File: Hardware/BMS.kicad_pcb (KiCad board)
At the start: 4 copper layers, 109 x 148 mm, 368 parts, among them IC1 STM32H742VIT6, IC2 TPS563200DDCR, J1 Conn_01x28, J10 Conn_01x10, J11 USB4235-03-C_REVA, J13 USB_A, J16 Conn_01x10, J19 Conn_02x13_Counter_Clockwise, J7 FTSH-107-01-L-D-K, Q2 100V/2W, Q5 DMT6018LDR-7, Q7 DMT6018LDR-7, Q8 100V/2W, SW1 SW_Push, U1 BQ79614PAPRQ1, U2 BQ79614PAPRQ1, U3 PBQ79600PWQ1, U4 MCP2542FD-E/MF, U5 PTPSM863253RDXR

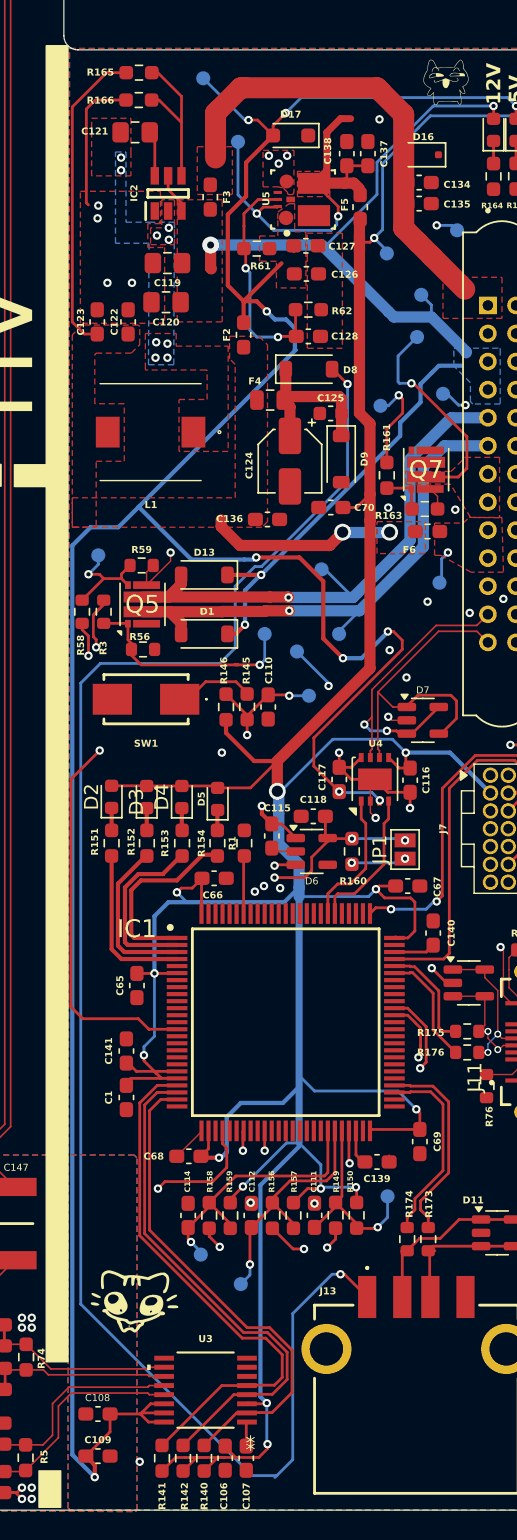
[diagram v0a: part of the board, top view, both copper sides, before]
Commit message: Dodano logikę ładowania bateri, zabezpieczenia OV UV na przekaźniku działają poprawnie, przekaźnik ma swój test polegający na styku pomocniczym
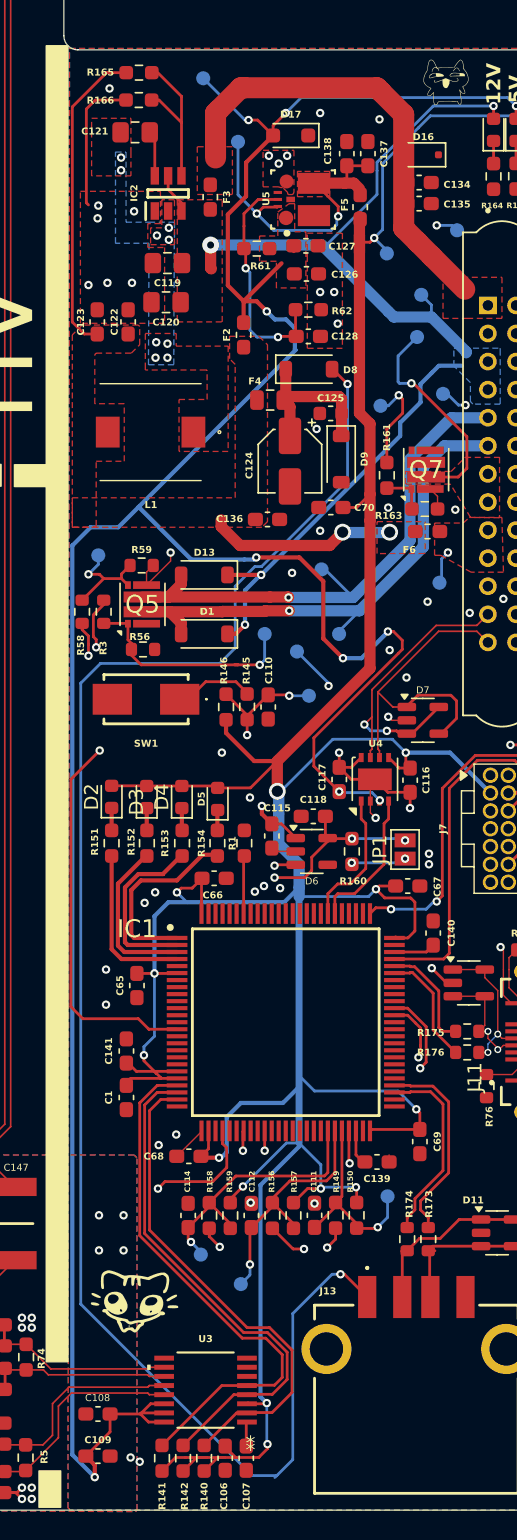
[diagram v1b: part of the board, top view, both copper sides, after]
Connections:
- R1 pad 1: Net-(R1-Pad1) -> GND
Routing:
- net Net-(U5-FB): track 29.1 -> 23.0 mm
- net GND: vias 43 -> 67
